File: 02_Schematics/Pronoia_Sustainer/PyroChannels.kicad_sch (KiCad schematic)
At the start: 35 parts, among them J10 Screw_Terminal_01x02, J11 Screw_Terminal_01x02, J3 Screw_Terminal_01x02, J8 Screw_Terminal_01x02, J9 Screw_Terminal_01x02, Q1 Q_NMOS, Q2 Q_NMOS, Q3 Q_NMOS, Q4 Q_NMOS, Q5 Q_NMOS

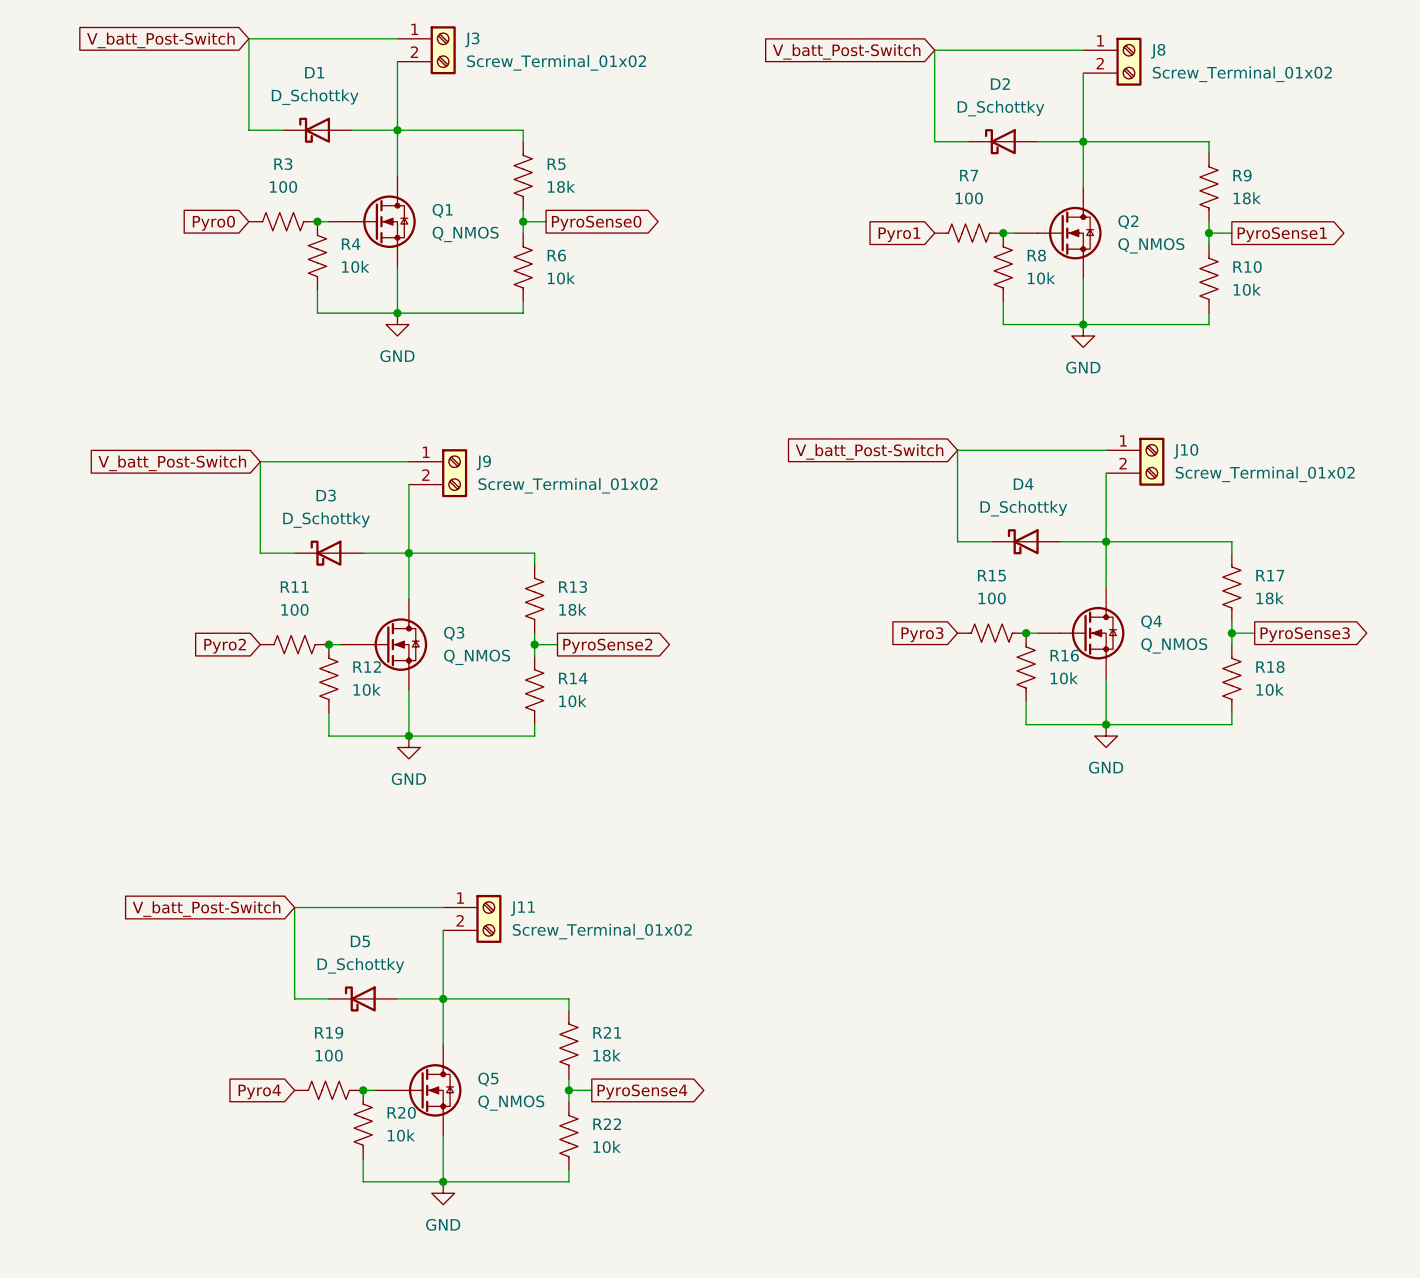
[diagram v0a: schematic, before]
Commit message: Added footprints to all placed symbols
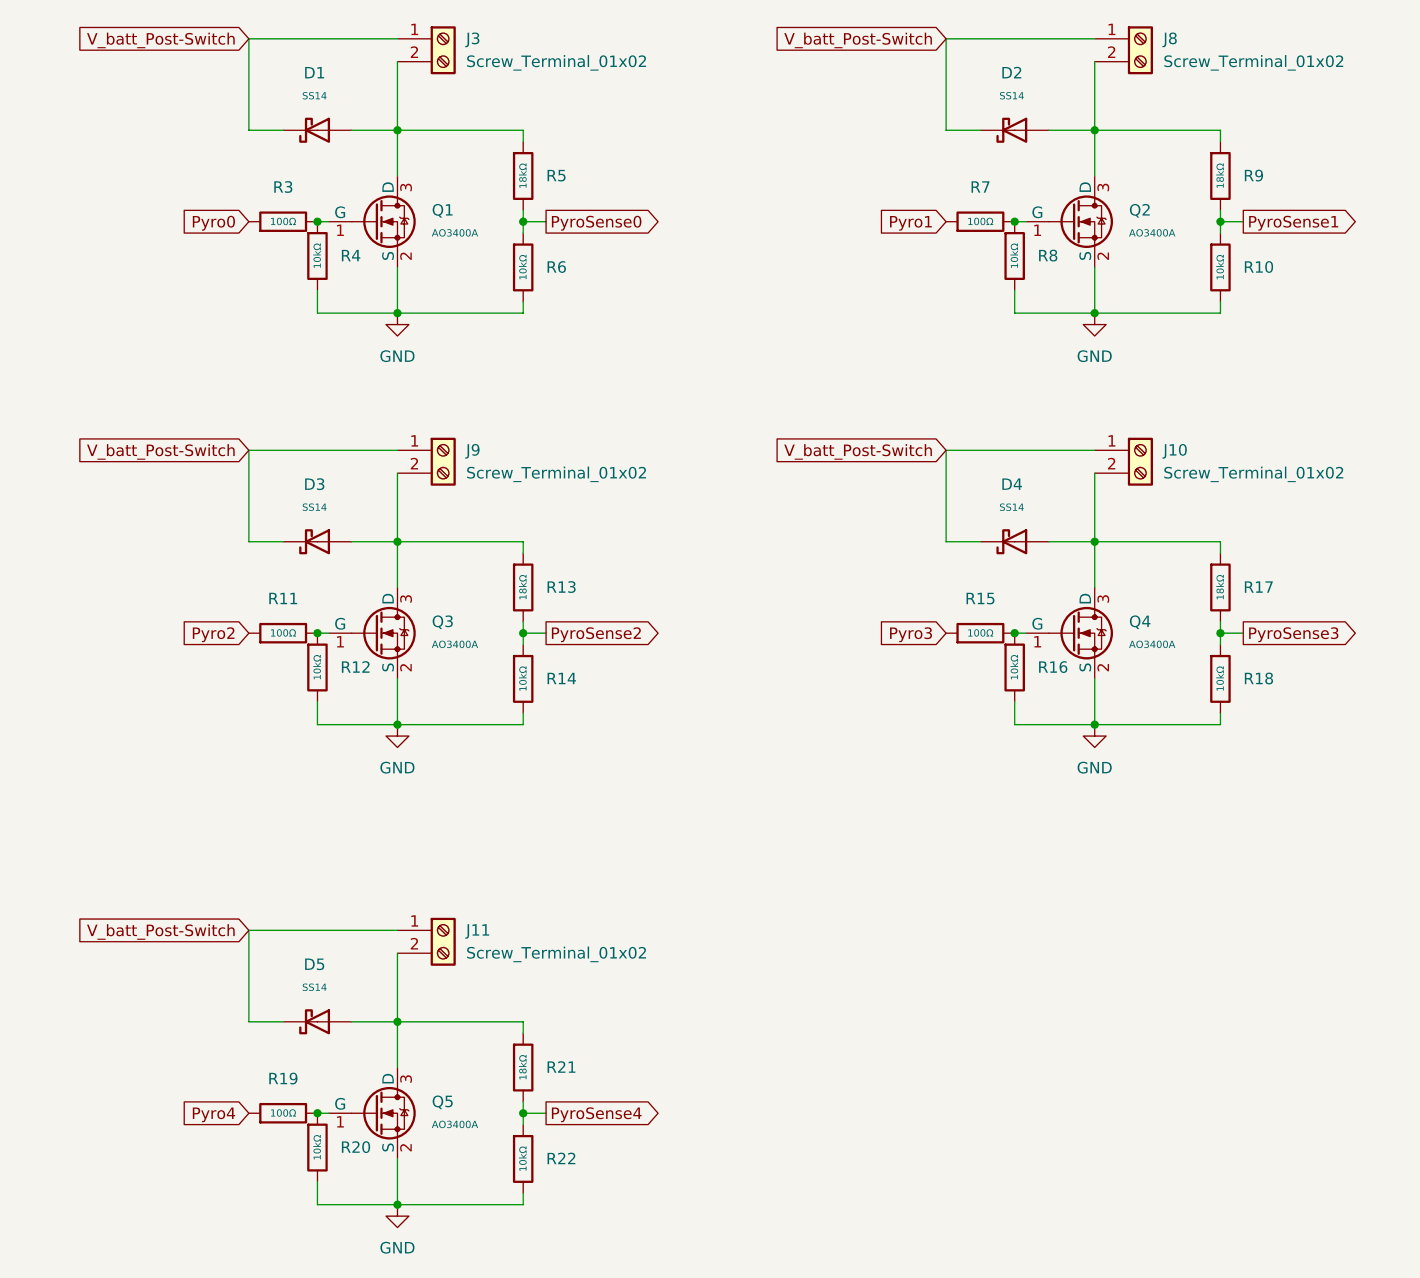
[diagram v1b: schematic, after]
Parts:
- removed D1, D2, D3, D4, D5: D_Schottky, symbol Device:D_Schottky
- removed Q1, Q2, Q3, Q4, Q5: Q_NMOS, Package_TO_SOT_SMD:SOT-23-3, symbol Device:Q_NMOS
- removed R10, R12, R14, R16, R18, R20, R22, R4, R6, R8: 10k, symbol Device:R_US
- removed R11, R15, R19, R3, R7: 100, symbol Device:R_US
- removed R13, R17, R21, R5, R9: 18k, symbol Device:R_US
- added D1, D2, D3, D4, D5: SS14, PCM_JLCPCB:D_SMA, symbol PCM_JLCPCB-Diodes:Schottky,SS14
- added Q1, Q2, Q3, Q4, Q5: AO3400A, PCM_JLCPCB:Q_SOT-23, symbol PCM_JLCPCB-Transistors:NMOS,AO3400A
- added R10, R12, R14, R16, R18, R20, R22, R4, R6, R8: 10kΩ, PCM_JLCPCB:R_0805, symbol PCM_JLCPCB-Resistors:0805,10kΩ
- added R11, R15, R19, R3, R7: 100Ω, PCM_JLCPCB:R_0805, symbol PCM_JLCPCB-Resistors:0805,100Ω
- added R13, R17, R21, R5, R9: 18kΩ, PCM_JLCPCB:R_0805, symbol PCM_JLCPCB-Resistors:0805,18kΩ
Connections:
- net GND: now also Q1.2 (S), Q2.2 (S), Q3.2 (S), Q4.2 (S), Q5.2 (S), R10.2, R12.2, R14.2, R16.2, R18.2, R20.2, R22.2, R4.2, R6.2, R8.2
- net Pyro0: now also R3.1
- net Pyro1: now also R7.1
- net Pyro2: now also R11.1
- net Pyro3: now also R15.1
- net Pyro4: now also R19.1
- net PyroSense0: now also R5.2, R6.1
- net PyroSense1: now also R10.1, R9.2
- net PyroSense2: now also R13.2, R14.1
- net PyroSense3: now also R17.2, R18.1
- net PyroSense4: now also R21.2, R22.1
- net V_batt_Post-Switch: now also D1.1, D2.1, D3.1, D4.1, D5.1
- net at J9.2 (Pin_2): now also D3.2, Q3.3 (D), R13.1
- net at J11.2 (Pin_2): now also D5.2, Q5.3 (D), R21.1
- net at J3.2 (Pin_2): now also D1.2, Q1.3 (D), R5.1
- net at J10.2 (Pin_2): now also D4.2, Q4.3 (D), R17.1
- net at J8.2 (Pin_2): now also D2.2, Q2.3 (D), R9.1
- new net: Q2.1 (G), R7.2, R8.1
- new net: Q1.1 (G), R3.2, R4.1
- new net: Q5.1 (G), R19.2, R20.1
- new net: Q3.1 (G), R11.2, R12.1
- new net: Q4.1 (G), R15.2, R16.1
